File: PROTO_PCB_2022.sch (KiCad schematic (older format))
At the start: 14 parts, among them J1 ECU_EN_CONNECTION, K1 RT214012, K2 RT214012

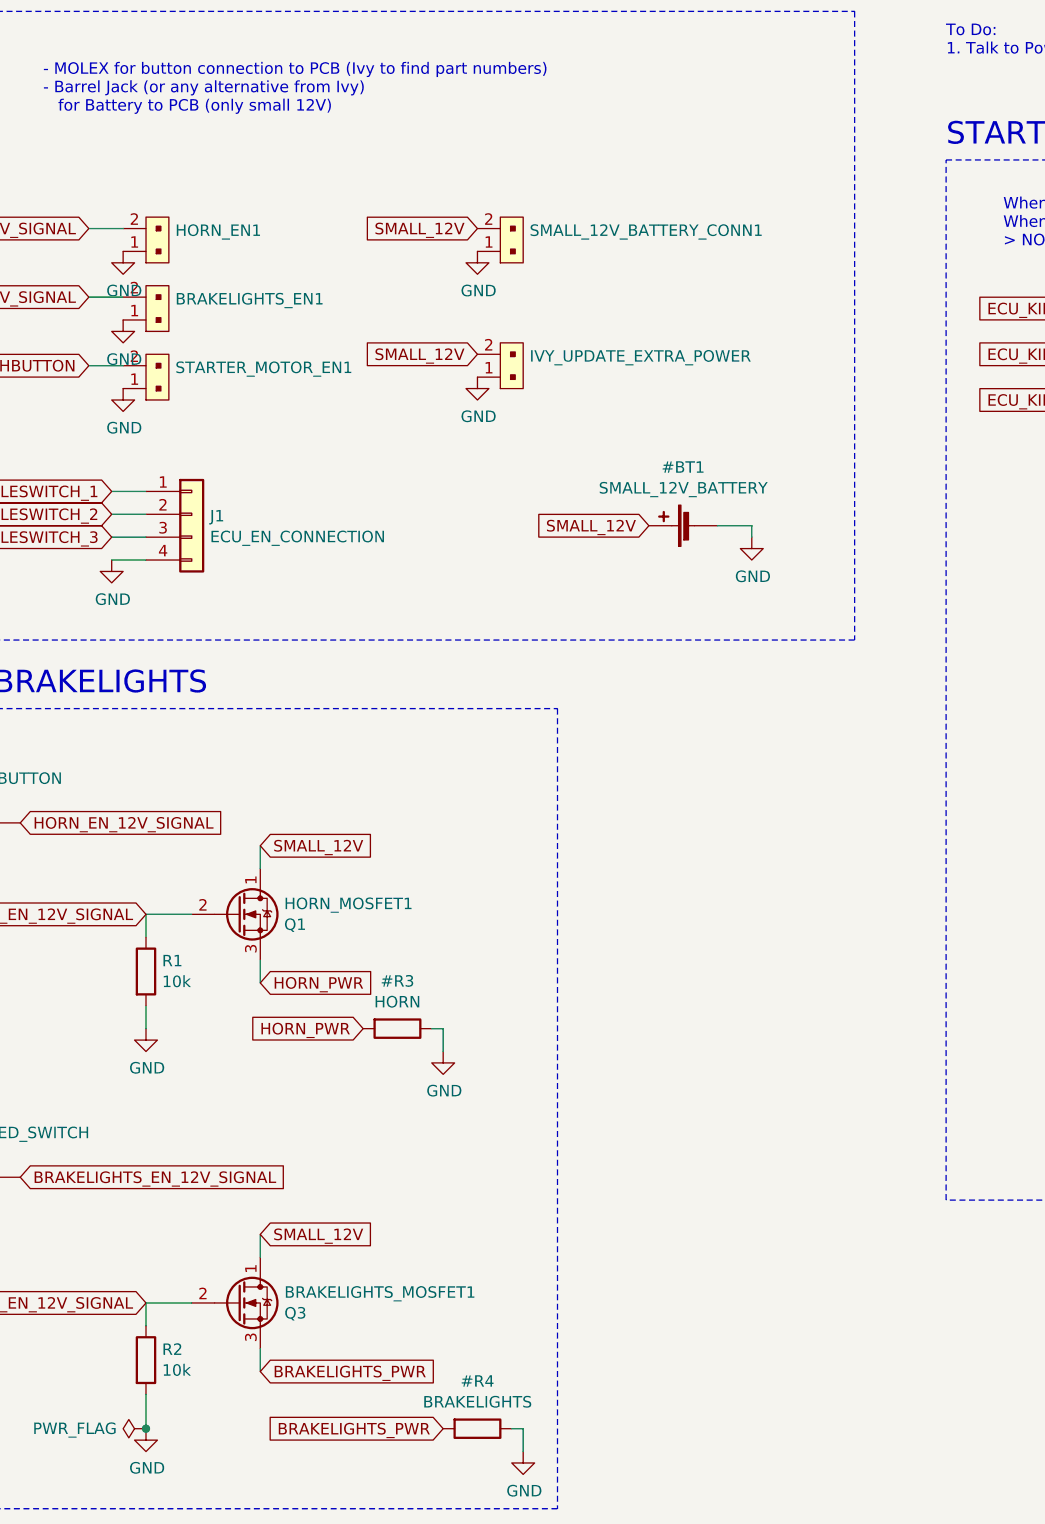
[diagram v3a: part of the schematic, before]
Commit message: Added footprints/PNs for connectors and updated resistors
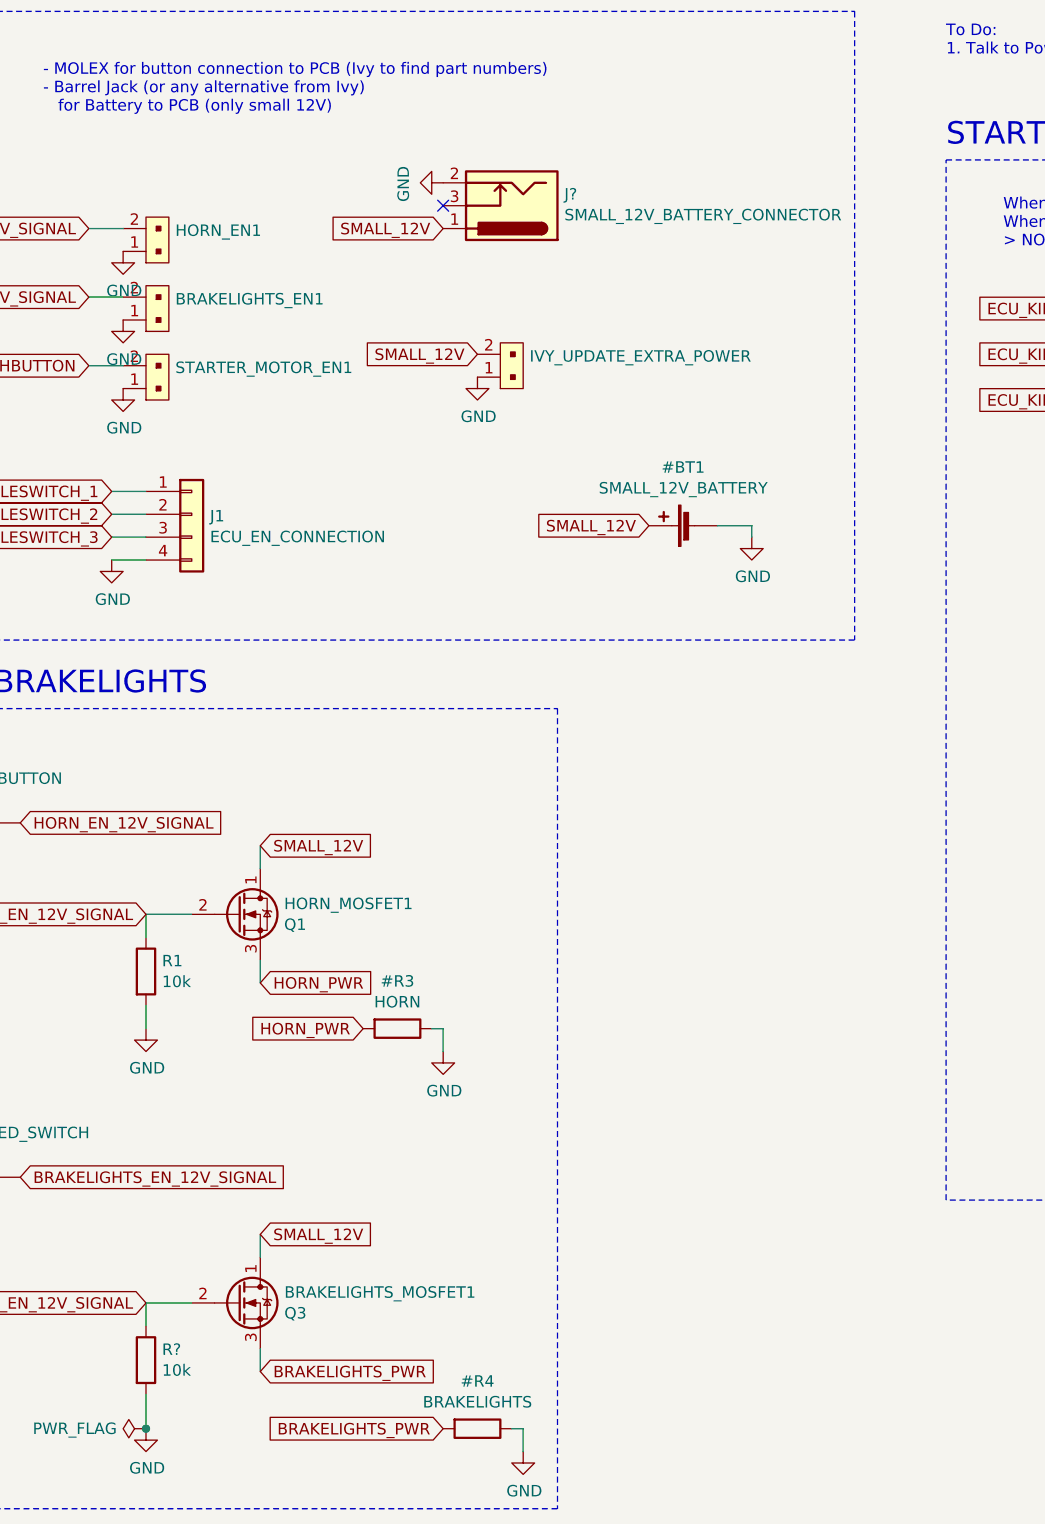
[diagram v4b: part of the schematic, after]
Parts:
- removed R2: 10k, Resistor_SMD:R_0402_1005Metric_Pad0.72x0.64mm_HandSolder, symbol Device:R
- removed SMALL_12V_BATTERY_CONN1: Conn_?, symbol PROTO_PCB_2022-rescue:B2B-PH-K-S_LF__SN_-dk_Rectangular-Connectors-Headers-Male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
- added J?: SMALL_12V_BATTERY_CONNECTOR, Connector_BarrelJack:BarrelJack_CUI_PJ-036AH-SMT_Horizontal, symbol Connector:Barrel_Jack_Switch
- added R?: 10k, Resistor_SMD:R_0805_2012Metric, symbol Device:R
- BRAKELIGHTS_EN1, STARTER_MOTOR_EN1: footprint (none) -> Connector_Molex:Molex_CLIK-Mate_502386-0270_1x02-1MP_P1.25mm_Horizontal; DigiKeyPN (none) -> WM4946CT-ND; MPN (none) -> 5023860270
- HORN_EN1: footprint Connector_Molex:Molex_CLIK-Mate_502443-0270_1x02-1MP_P2.00mm_Vertical -> Connector_Molex:Molex_CLIK-Mate_502386-0270_1x02-1MP_P1.25mm_Horizontal; DigiKeyPN WM10606CT-ND -> WM4946CT-ND; MPN 5033950410 -> 5023860270
- J1: footprint Connector_Molex:Molex_CLIK-Mate_505405-0470_1x04-1MP_P1.50mm_Vertical -> Connector_Molex:Molex_CLIK-Mate_502386-0470_1x04-1MP_P1.25mm_Horizontal; DigikeyPN (none) -> WM4948CT-ND; MPN (none) -> 5023860470
- R1: footprint Resistor_SMD:R_0402_1005Metric_Pad0.72x0.64mm_HandSolder -> Resistor_SMD:R_0805_2012Metric; DigikeyPN (none) -> 311-10.0CRCT-ND; MPN RC1005F103CS -> RC0805FR-0710RL
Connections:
- net BRAKELIGHTS_EN_12V_SIGNAL: now also R?.1
- net GND: now also J?.2, R?.2
- net SMALL_12V: now also J?.1
- no-connect marks 0 -> 1
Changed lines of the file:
@@
 STARTER_EN_PUSHBUTTON
-$Comp
-L Device:R R2
-U 1 1 619A0EBB
-P 2250 7000
-F 0 "R2" H 2320 7046 50  0000 L CNN
-F 1 "10k" H 2320 6955 50  0000 L CNN
-F 2 "Resistor_SMD:R_0402_1005Metric_Pad0.72x0.64mm_HandSolder" V 2180 7000 50  0001 C CNN
-F 3 "https://media.digikey.com/pdf/Data%20Sheets/Samsung%20PDFs/RC_Series_ds.pdf" H 2250 7000 50  0001 C CNN
-F 4 "RC1005F103CS" H 2250 7000 50  0001 C CNN "MPN"
-	1    2250 7000
-	1    0    0    -1
-$EndComp
 $Comp
 L power:GND #PWR05
@@
 F 0 "R1" H 2320 5346 50  0000 L CNN
 F 1 "10k" H 2320 5255 50  0000 L CNN
-F 2 "Resistor_SMD:R_0402_1005Metric_Pad0.72x0.64mm_HandSolder" V 2180 5300 50  0001 C CNN
-F 3 "https://media.digikey.com/pdf/Data%20Sheets/Samsung%20PDFs/RC_Series_ds.pdf" H 2250 5300 50  0001 C CNN
-F 4 "RC1005F103CS" H 2250 5300 50  0001 C CNN "MPN"
+F 2 "Resistor_SMD:R_0805_2012Metric" V 2180 5300 50  0001 C CNN
+F 3 "https://www.yageo.com/upload/media/product/productsearch/datasheet/rchip/PYu-RC_Group_51_RoHS_L_11.pdf" H 2250 5300 50  0001 C CNN
+F 4 "RC0805FR-0710RL" H 2250 5300 50  0001 C CNN "MPN"
+F 5 "311-10.0CRCT-ND" H 2250 5300 50  0001 C CNN "DigikeyPN"
 	1    2250 5300
 	1    0    0    -1
@@
 Wire Wire Line
 	2450 5050 2250 5050
-$Comp
-L Device:R #R3
-U 1 1 61E64182
-P 3350 5550
-F 0 "#R3" V 3143 5550 50  0000 C CNN
-F 1 "HORN" V 3234 5550 50  0000 C CNN
-F 2 "" V 3280 5550 50  0001 C CNN
-F 3 "~" H 3350 5550 50  0001 C CNN
-	1    3350 5550
-	0    1    1    0
-$EndComp
 Text GLabel 2750 5350 2    50   Input ~ 0
 HORN_PWR
@@
 F 0 "HORN_EN1" V 2341 2022 50  0000 R CNN
 F 1 "Conn_?" V 2250 2022 50  0001 R CNN
-F 2 "Connector_Molex:Molex_CLIK-Mate_502443-0270_1x02-1MP_P2.00mm_Vertical" H 2450 2350 60  0001 L CNN
-F 3 "http://www.literature.molex.com/SQLImages/kelmscott/Molex/PDF_Images/987650-3302.PDF" H 2450 2450 60  0001 L CNN
-F 4 "WM10606CT-ND" H 2450 2550 60  0001 L CNN "DigiKeyPN"
-F 5 "5033950410" H 2450 2650 60  0001 L CNN "MPN"
+F 2 "Connector_Molex:Molex_CLIK-Mate_502386-0270_1x02-1MP_P1.25mm_Horizontal" H 2450 2350 60  0001 L CNN
+F 3 "https://www.molex.com/pdm_docs/sd/5023860270_sd.pdf" H 2450 2450 60  0001 L CNN
+F 4 "WM4946CT-ND" H 2450 2550 60  0001 L CNN "DigiKeyPN"
+F 5 "5023860270" H 2450 2650 60  0001 L CNN "MPN"
 	1    2250 2150
-	0    -1   -1   0
-$EndComp
-$Comp
-L PROTO_PCB_2022-rescue:B2B-PH-K-S_LF__SN_-dk_Rectangular-Connectors-Headers-Male-Pins-Proto-PCB's-combined-rescue-Proto-PCB's-combined-rescue BRAKELIGHTS_EN1
-U 1 1 61ECDF47
-P 2250 2450
-F 0 "BRAKELIGHTS_EN1" V 2341 2322 50  0000 R CNN
-F 1 "Conn_?" V 2250 2322 50  0001 R CNN
-F 2 "" H 2450 2650 60  0001 L CNN
-F 3 "" H 2450 2750 60  0001 L CNN
-F 4 "" H 2450 2850 60  0001 L CNN "DigiKeyPN"
-F 5 "" H 2450 2950 60  0001 L CNN "MPN"
-	1    2250 2450
-	0    -1   -1   0
-$EndComp
-$Comp
-L PROTO_PCB_2022-rescue:B2B-PH-K-S_LF__SN_-dk_Rectangular-Connectors-Headers-Male-Pins-Proto-PCB's-combined-rescue-Proto-PCB's-combined-rescue STARTER_MOTOR_EN1
-U 1 1 61ECE961
-P 2250 2750
-F 0 "STARTER_MOTOR_EN1" V 2341 2622 50  0000 R CNN
-F 1 "Conn_?" V 2250 2622 50  0001 R CNN
-F 2 "" H 2450 2950 60  0001 L CNN
-F 3 "" H 2450 3050 60  0001 L CNN
-F 4 "" H 2450 3150 60  0001 L CNN "DigiKeyPN"
-F 5 "" H 2450 3250 60  0001 L CNN "MPN"
-	1    2250 2750
 	0    -1   -1   0
 $EndComp
@@
 Text Notes 1800 1550 0    50   ~ 0
 - MOLEX for button connection to PCB (Ivy to find part numbers)\n- Barrel Jack (or any alternative from Ivy) \n   for Battery to PCB (only small 12V)
-$Comp
-L power:GND #PWR08
-U 1 1 61EE358E
-P 3700 2150
-F 0 "#PWR08" H 3700 1900 50  0001 C CNN
-F 1 "GND" H 3705 1977 50  0000 C CNN
-F 2 "" H 3700 2150 50  0001 C CNN
-F 3 "" H 3700 2150 50  0001 C CNN
-	1    3700 2150
-	1    0    0    -1
-$EndComp
-Text GLabel 3700 2050 0    50   Input ~ 0
+Text GLabel 3550 2050 0    50   Input ~ 0
 SMALL_12V
 $Comp
@@
 POWER AND CONNECTIONS\n
 $Comp
-L PROTO_PCB_2022-rescue:B2B-PH-K-S_LF__SN_-dk_Rectangular-Connectors-Headers-Male-Pins-Proto-PCB's-combined-rescue-Proto-PCB's-combined-rescue SMALL_12V_BATTERY_CONN1
-U 1 1 61ECC655
-P 3800 2150
-F 0 "SMALL_12V_BATTERY_CONN1" V 3891 2022 50  0000 R CNN
-F 1 "Conn_?" V 3800 2022 50  0001 R CNN
-F 2 "" H 4000 2350 60  0001 L CNN
-F 3 "" H 4000 2450 60  0001 L CNN
-F 4 "" H 4000 2550 60  0001 L CNN "DigiKeyPN"
-F 5 "" H 4000 2650 60  0001 L CNN "MPN"
-	1    3800 2150
-	0    -1   -1   0
-$EndComp
-$Comp
 L Connector_Generic:Conn_01x04 J1
 U 1 1 61E4C7B0
@@
 F 0 "J1" H 2530 3292 50  0000 L CNN
 F 1 "ECU_EN_CONNECTION" H 2530 3201 50  0000 L CNN
-F 2 "Connector_Molex:Molex_CLIK-Mate_505405-0470_1x04-1MP_P1.50mm_Vertical" H 2450 3300 50  0001 C CNN
-F 3 "~" H 2450 3300 50  0001 C CNN
+F 2 "Connector_Molex:Molex_CLIK-Mate_502386-0470_1x04-1MP_P1.25mm_Horizontal" H 2450 3300 50  0001 C CNN
+F 3 "4 Position Receptacle Connector 0.049\" (1.25mm) Surface Mount, Right Angle Tin" H 2450 3300 50  0001 C CNN
+F 4 "WM4948CT-ND" H 2450 3300 50  0001 C CNN "DigikeyPN"
+F 5 "5023860470" H 2450 3300 50  0001 C CNN "MPN"
 	1    2450 3300
 	1    0    0    -1
@@
 Wire Notes Line
 	800  7650 800  4150
+$Comp
+L Connector:Barrel_Jack_Switch J?
+U 1 1 61E7CEA3
+P 3850 1950
+F 0 "J?" H 3620 1900 50  0000 R CNN
+F 1 "SMALL_12V_BATTERY_CONNECTOR" H 3620 1991 50  0000 R CNN
+F 2 "Connector_BarrelJack:BarrelJack_CUI_PJ-036AH-SMT_Horizontal" H 3900 1910 50  0001 C CNN
+F 3 "https://www.cuidevices.com/product/resource/pj-036ah-smt-tr.pdf" H 3900 1910 50  0001 C CNN
+F 4 "CP-036AHPJCT-ND" H 3850 1950 50  0001 C CNN "DigikeyPN"
+F 5 "PJ-036AH-SMT-TR" H 3850 1950 50  0001 C CNN "MPN"
+	1    3850 1950
+	-1   0    0    1
+$EndComp
+$Comp
+L power:GND #PWR08
+U 1 1 61EE358E
+P 3550 1850
+F 0 "#PWR08" H 3550 1600 50  0001 C CNN
+F 1 "GND" H 3555 1677 50  0000 C CNN
+F 2 "" H 3550 1850 50  0001 C CNN
+F 3 "" H 3550 1850 50  0001 C CNN
+	1    3550 1850
+	0    1    1    0
+$EndComp
+NoConn ~ 3550 1950
+$Comp
+L PROTO_PCB_2022-rescue:B2B-PH-K-S_LF__SN_-dk_Rectangular-Connectors-Headers-Male-Pins-Proto-PCB's-combined-rescue-Proto-PCB's-combined-rescue BRAKELIGHTS_EN1
+U 1 1 61E8C377
+P 2250 2450
+F 0 "BRAKELIGHTS_EN1" V 2341 2322 50  0000 R CNN
+F 1 "Conn_?" V 2250 2322 50  0001 R CNN
+F 2 "Connector_Molex:Molex_CLIK-Mate_502386-0270_1x02-1MP_P1.25mm_Horizontal" H 2450 2650 60  0001 L CNN
+F 3 "https://www.molex.com/pdm_docs/sd/5023860270_sd.pdf" H 2450 2750 60  0001 L CNN
+F 4 "WM4946CT-ND" H 2450 2850 60  0001 L CNN "DigiKeyPN"
+F 5 "5023860270" H 2450 2950 60  0001 L CNN "MPN"
+	1    2250 2450
+	0    -1   -1   0
+$EndComp
+$Comp
+L PROTO_PCB_2022-rescue:B2B-PH-K-S_LF__SN_-dk_Rectangular-Connectors-Headers-Male-Pins-Proto-PCB's-combined-rescue-Proto-PCB's-combined-rescue STARTER_MOTOR_EN1
+U 1 1 61E8EEF4
+P 2250 2750
+F 0 "STARTER_MOTOR_EN1" V 2341 2622 50  0000 R CNN
+F 1 "Conn_?" V 2250 2622 50  0001 R CNN
+F 2 "Connector_Molex:Molex_CLIK-Mate_502386-0270_1x02-1MP_P1.25mm_Horizontal" H 2450 2950 60  0001 L CNN
+F 3 "https://www.molex.com/pdm_docs/sd/5023860270_sd.pdf" H 2450 3050 60  0001 L CNN
+F 4 "WM4946CT-ND" H 2450 3150 60  0001 L CNN "DigiKeyPN"
+F 5 "5023860270" H 2450 3250 60  0001 L CNN "MPN"
+	1    2250 2750
+	0    -1   -1   0
+$EndComp
+$Comp
+L Device:R #R3
+U 1 1 61E64182
+P 3350 5550
+F 0 "#R3" V 3143 5550 50  0000 C CNN
+F 1 "HORN" V 3234 5550 50  0000 C CNN
+F 2 "" V 3280 5550 50  0001 C CNN
+F 3 "~" H 3350 5550 50  0001 C CNN
+	1    3350 5550
+	0    1    1    0
+$EndComp
+$Comp
+L Device:R R?
+U 1 1 61E941D5
+P 2250 7000
+F 0 "R?" H 2320 7046 50  0000 L CNN
+F 1 "10k" H 2320 6955 50  0000 L CNN
+F 2 "Resistor_SMD:R_0805_2012Metric" V 2180 7000 50  0001 C CNN
+F 3 "https://www.yageo.com/upload/media/product/productsearch/datasheet/rchip/PYu-RC_Group_51_RoHS_L_11.pdf" H 2250 7000 50  0001 C CNN
+F 4 "RC0805FR-0710RL" H 2250 7000 50  0001 C CNN "MPN"
+F 5 "311-10.0CRCT-ND" H 2250 7000 50  0001 C CNN "DigikeyPN"
+	1    2250 7000
+	1    0    0    -1
+$EndComp
 $EndSCHEMATC
